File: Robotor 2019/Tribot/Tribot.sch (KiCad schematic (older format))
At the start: 63 parts, among them M1 Motor_DC, M2 Motor_DC, SW1 SW_Push, U1 AMS1117-3V3, U2 AMS1117-3V3, U3 AMS1117-5.0, Y1 Crystal, Y2 Crystal

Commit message: Nici nu mai stiu, am facut la scoala pe data de 23.07
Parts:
- removed C? (x2): 0.1uF, symbol Device:CP
- removed J?: Conn_01x04_Male, symbol Connector:Conn_01x04_Male
- added C3, C8: 100n, Capacitor_SMD:C_0805_2012Metric_Pad1.15x1.40mm_HandSolder, symbol Device:C
- added D9: LED, LED_SMD:LED_0805_2012Metric_Pad1.15x1.40mm_HandSolder, symbol Device:LED
- added J4, J5, J6: Conn_01x04_Female, symbol Connector:Conn_01x04_Female
- added J7, J8: Conn_01x03_Female, symbol Connector:Conn_01x03_Female
- added R20: 10K, Resistor_SMD:R_0805_2012Metric_Pad1.15x1.40mm_HandSolder, symbol Device:R
- added R5, R7: 1K, Resistor_SMD:R_0805_2012Metric_Pad1.15x1.40mm_HandSolder, symbol Device:R
- C1, C2, C4, C5, C6, C7, C9: footprint (none) -> Capacitor_SMD:C_0805_2012Metric_Pad1.15x1.40mm_HandSolder
- C12, C13, C15, C17, C18, C21, CP6: renamed from C?; footprint (none) -> Capacitor_SMD:C_0805_2012Metric_Pad1.15x1.40mm_HandSolder
- CP1: renamed from C?; footprint (none) -> Capacitor_SMD:CP_Elec_4x5.3
- CP2: renamed from C8; footprint (none) -> Capacitor_SMD:CP_Elec_6.3x7.7
- CP3, CP5: renamed from C?; footprint (none) -> Capacitor_SMD:CP_Elec_6.3x7.7
- CP4: renamed from C3; footprint (none) -> Capacitor_SMD:CP_Elec_6.3x7.7
- D1, D2, D3, D4, D5, D6, D7, D8: renamed from D?; footprint (none) -> Diode_SMD:D_0805_2012Metric_Pad1.15x1.40mm_HandSolder
- J1: renamed from J?; footprint (none) -> Connector_Wire:SolderWirePad_1x03_P5.715mm_Drill2mm
- R1, R10, R11, R2, R3, R4, R6, R8, R9: footprint (none) -> Resistor_SMD:R_0805_2012Metric_Pad1.15x1.40mm_HandSolder
- R12, R13, R14, R15, R16, R17, R18, R19: renamed from R?; footprint (none) -> Resistor_SMD:R_0805_2012Metric_Pad1.15x1.40mm_HandSolder
- SW1: footprint (none) -> Button_Switch_THT:SW_PUSH_6mm
- Y1, Y2: footprint (none) -> Crystal:Crystal_SMD_SeikoEpson_MA505-2Pin_12.7x5.1mm
- gave numbers to parts that had none: 7
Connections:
- net labels added: H1, H2, US1_IN, US1_OUT, US2_IN, US2_OUT, US3_IN, US3_OUT
- net labels removed: CLK, DIO
- wire segments 199 -> 228
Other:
- moved on the sheet: C12, CP1, J3, R10, R11, R3, R9, U2

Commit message: Assigned footprints to all parts. Arranged sensors in PCB schematic.
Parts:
- removed SW1: SW_Push, Button_Switch_THT:SW_PUSH_6mm, symbol Switch:SW_Push
- added J2: Conn_01x04_Female, Connector_PinSocket_2.54mm:PinSocket_1x04_P2.54mm_Vertical, symbol Connector:Conn_01x04_Female
- added JP1, JP2: Jumper, Connector_PinSocket_2.54mm:PinSocket_1x02_P2.54mm_Vertical, symbol Device:Jumper
- C15, C17, C18, C21: value C -> 10n
- CP2, CP3, CP4, CP5: footprint Capacitor_SMD:CP_Elec_6.3x7.7 -> Capacitor_SMD:CP_Elec_4x5.3
- CP6: footprint Capacitor_SMD:C_0805_2012Metric_Pad1.15x1.40mm_HandSolder -> Capacitor_SMD:CP_Elec_4x5.3
- D1, D2, D3, D4, D5, D6, D7, D8: footprint Diode_SMD:D_0805_2012Metric_Pad1.15x1.40mm_HandSolder -> Diode_THT:D_DO-15_P5.08mm_Vertical_AnodeUp
- J3: footprint (none) -> Connector_USB:USB_Mini-B_Lumberg_2486_01_Horizontal
- J4, J5, J6: footprint (none) -> Connector_PinHeader_2.54mm:PinHeader_1x04_P2.54mm_Vertical
- J7, J8: footprint (none) -> Connector_PinHeader_2.54mm:PinHeader_1x03_P2.54mm_Vertical
- M1, M2: footprint (none) -> Connector_Wire:SolderWirePad_1x02_P5.08mm_Drill1.5mm
- R12, R13, R14, R15, R16, R17, R18, R19: value R -> 220
- R20: value 10K -> R
- U6: footprint (none) -> Package_SO:HSOP-20-1EP_11.0x15.9mm_P1.27mm_SlugUp
- Y1: value Crystal -> 32.768Khz
- Y2: value Crystal -> 8Mhz
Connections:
- net labels added: BOOT1, CLK, DIO
- net labels removed: -5V
- wire segments 228 -> 231
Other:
- moved on the sheet: J8, R7

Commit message: The PCB for Tribot up to the point we realised we need a 2nd floor.
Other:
- moved on the sheet: C3, C8, CP5, CP6, D1, D2, D3, D4, D5, D6, D7, D8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

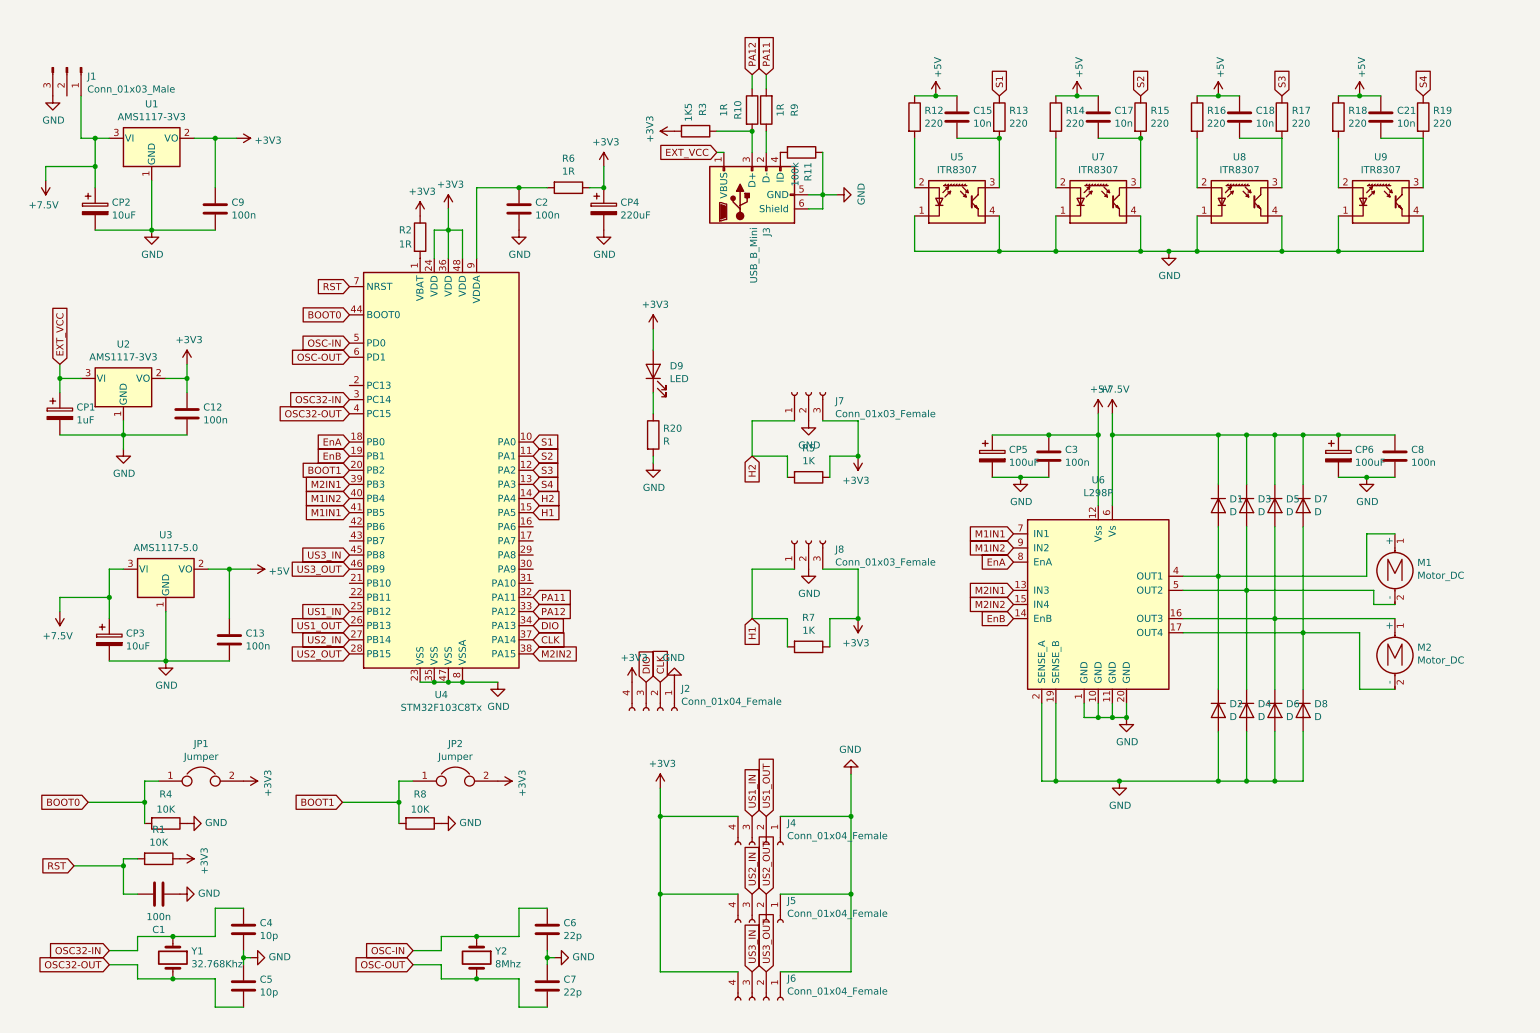
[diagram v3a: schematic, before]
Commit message: Updated electric schematic for tribot with 2 floors.
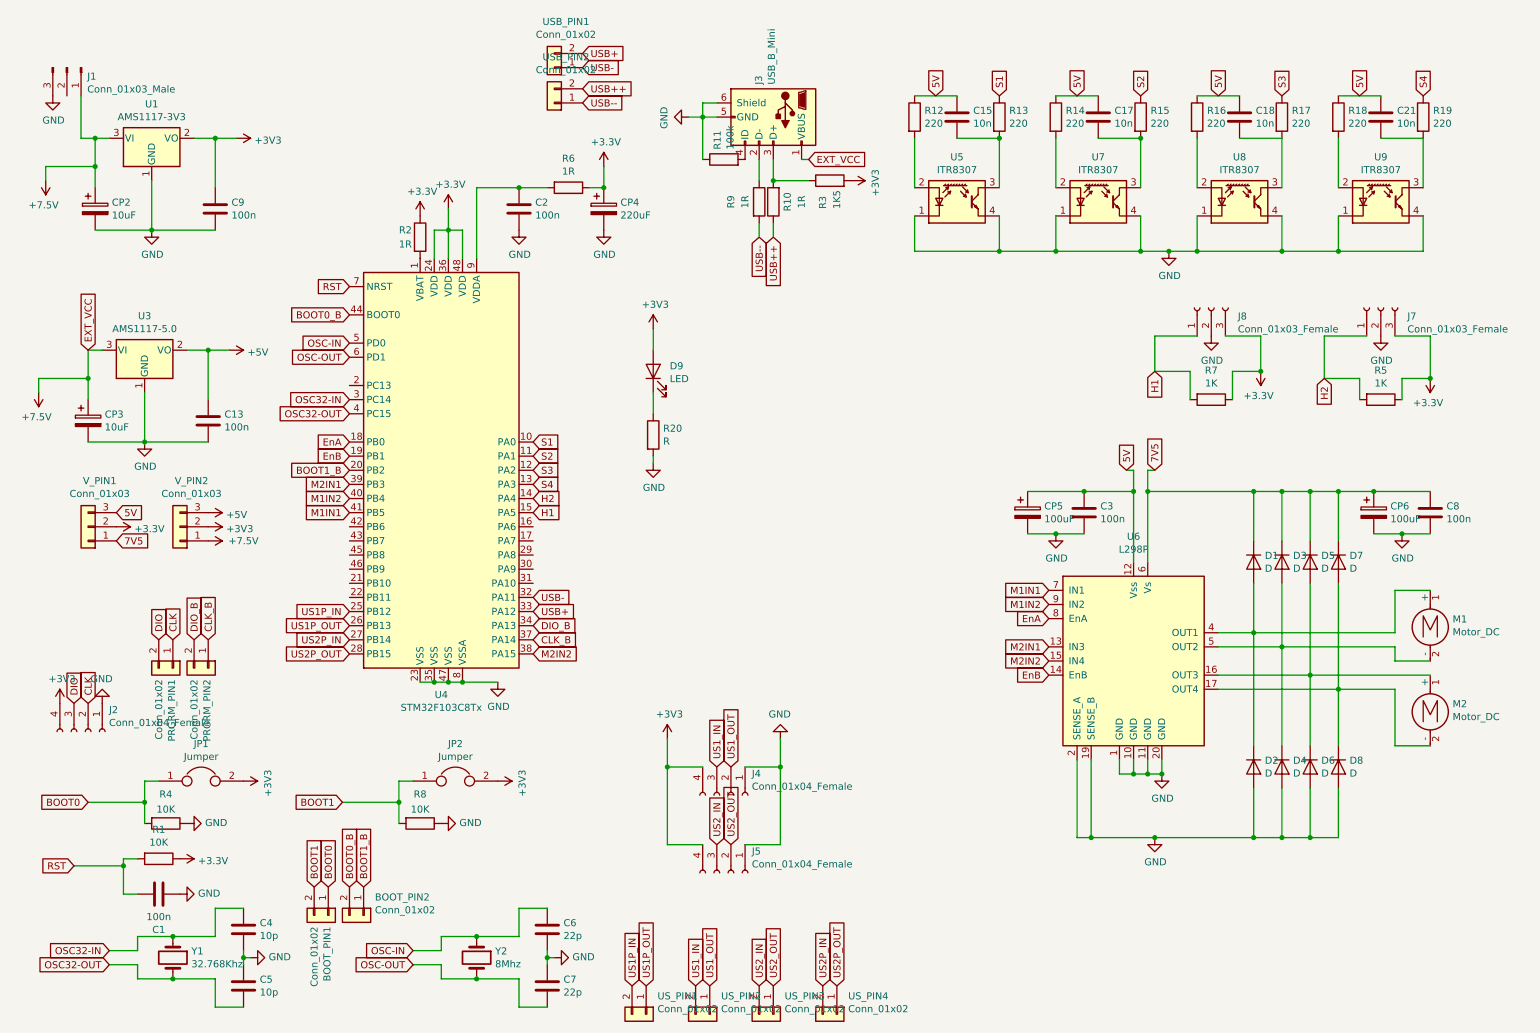
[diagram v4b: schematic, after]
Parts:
- removed C12: 100n, Capacitor_SMD:C_0805_2012Metric_Pad1.15x1.40mm_HandSolder, symbol Device:C
- removed CP1: 1uF, Capacitor_SMD:CP_Elec_4x5.3, symbol Device:CP
- removed J6: Conn_01x04_Female, Connector_PinHeader_2.54mm:PinHeader_1x04_P2.54mm_Vertical, symbol Connector:Conn_01x04_Female
- removed U2: AMS1117-3V3, Package_TO_SOT_SMD:SOT-223-3_TabPin2, symbol Regulator_Linear:AMS1117-5.0
- added BOOT_PIN1, BOOT_PIN2, PRGRM_PIN1, PRGRM_PIN2, USB_PIN1, USB_PIN2, US_PIN1, US_PIN2, US_PIN3, US_PIN4: Conn_01x02, Connector_PinHeader_2.54mm:PinHeader_1x02_P2.54mm_Vertical, symbol Connector_Generic:Conn_01x02
- added V_PIN1, V_PIN2: Conn_01x03, Connector_Wire:SolderWirePad_1x03_P5.715mm_Drill2mm, symbol Connector_Generic:Conn_01x03
- D1, D2, D3, D4, D5, D6, D7, D8: footprint Diode_THT:D_DO-15_P5.08mm_Vertical_AnodeUp -> Diode_THT:D_A-405_P5.08mm_Vertical_AnodeUp
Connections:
- net EXT_VCC is gone; now on net +7.5V: J3.1 (VBUS)
- net +3V3: now also V_PIN1.2 (Pin_2), V_PIN2.2 (Pin_2)
- net +5V: now also V_PIN2.3 (Pin_3); no longer C15.1, C17.1, C18.1, C21.1, C3.1, CP5.1, R12.1, R14.1, R16.1, R18.1, U6.12 (Vss)
- net +7.5V: now also V_PIN2.1 (Pin_1); no longer C8.1, CP6.1, D1.1 (K), D3.1 (K), D5.1 (K), D7.1 (K), U6.6 (Vs)
- net BOOT0: now also BOOT_PIN1.1 (Pin_1); no longer U4.44 (BOOT0)
- net BOOT1: now also BOOT_PIN1.2 (Pin_2); no longer U4.20 (PB2)
- net CLK: now also PRGRM_PIN1.1 (Pin_1); no longer U4.37 (PA14)
- net DIO: now also PRGRM_PIN1.2 (Pin_2); no longer U4.34 (PA13)
- net US1_IN: now also US_PIN2.2 (Pin_2); no longer U4.25 (PB12)
- net US1_OUT: now also US_PIN2.1 (Pin_1); no longer U4.26 (PB13)
- net US2_IN: now also US_PIN3.2 (Pin_2); no longer U4.27 (PB14)
- net US2_OUT: now also US_PIN3.1 (Pin_1); no longer U4.28 (PB15)
- net PA11 renamed USB-
- net USB-: now also USB_PIN1.1 (Pin_1); no longer R9.2
- net PA12 renamed USB+
- net USB+: now also USB_PIN1.2 (Pin_2); no longer R10.1
- net US3_IN: no longer names the net of U4.45 (PB8)
- net US3_OUT: no longer names the net of U4.46 (PB9)
- new net 5V: C15.1, C17.1, C18.1, C21.1, C3.1, CP5.1, R12.1, R14.1, R16.1, R18.1, U6.12 (Vss), V_PIN1.3 (Pin_3)
- new net 7V5: C8.1, CP6.1, D1.1 (K), D3.1 (K), D5.1 (K), D7.1 (K), U6.6 (Vs), V_PIN1.1 (Pin_1)
- new net BOOT0_B: BOOT_PIN2.2 (Pin_2), U4.44 (BOOT0)
- new net BOOT1_B: BOOT_PIN2.1 (Pin_1), U4.20 (PB2)
- new net CLK_B: PRGRM_PIN2.1 (Pin_1), U4.37 (PA14)
- new net DIO_B: PRGRM_PIN2.2 (Pin_2), U4.34 (PA13)
- new net US1P_IN: U4.25 (PB12), US_PIN1.2 (Pin_2)
- new net US1P_OUT: U4.26 (PB13), US_PIN1.1 (Pin_1)
- new net US2P_IN: U4.27 (PB14), US_PIN4.2 (Pin_2)
- new net US2P_OUT: U4.28 (PB15), US_PIN4.1 (Pin_1)
- new net USB++: R10.1, USB_PIN2.2 (Pin_2)
- new net USB--: R9.2, USB_PIN2.1 (Pin_1)
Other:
- moved on the sheet: C13, C3, C8, CP3, CP5, CP6, D1, D2, D3, D4, D5, D6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

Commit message: Bottom tribot circuit board.
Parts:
- removed V_PIN1, V_PIN2: Conn_01x03, Connector_Wire:SolderWirePad_1x03_P5.715mm_Drill2mm, symbol Connector_Generic:Conn_01x03
- added M_PIN1, M_PIN2, M_PIN3, M_PIN4: Conn_01x03, Connector_PinSocket_2.54mm:PinSocket_1x03_P2.54mm_Vertical, symbol Connector_Generic:Conn_01x03
- added V_PIN1, V_PIN2: Conn_01x02, Connector_Wire:SolderWirePad_1x02_P5.08mm_Drill1.5mm, symbol Connector_Generic:Conn_01x02
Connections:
- net 7V5 is gone; now on net +7.5V: C8.1, CP6.1, D1.1 (K), D3.1 (K), D5.1 (K), D7.1 (K), U6.6 (Vs)
- net +3V3: now also V_PIN2.1 (Pin_1); no longer CP4.1, J7.3 (Pin_3), J8.3 (Pin_3), R1.1, R2.1, R5.1, R6.1, R7.1, U4.24 (VDD), U4.36 (VDD), U4.48 (VDD)
- net +5V: now also C3.1, CP5.1, U6.12 (Vss), V_PIN2.2 (Pin_2)
- net 5V: now also V_PIN1.2 (Pin_2); no longer C3.1, CP5.1, U6.12 (Vss)
- net EnA: now also M_PIN2.1 (Pin_1); no longer U4.18 (PB0)
- net EnB: now also M_PIN4.1 (Pin_1); no longer U4.19 (PB1)
- net M1IN1: now also M_PIN2.2 (Pin_2); no longer U4.41 (PB5)
- net M1IN2: now also M_PIN2.3 (Pin_3); no longer U4.40 (PB4)
- net M2IN1: now also M_PIN4.2 (Pin_2); no longer U4.39 (PB3)
- net M2IN2: now also M_PIN4.3 (Pin_3); no longer U4.38 (PA15)
- new net 3V3: CP4.1, J7.3 (Pin_3), J8.3 (Pin_3), R1.1, R2.1, R5.1, R6.1, R7.1, U4.24 (VDD), U4.36 (VDD), U4.48 (VDD), V_PIN1.1 (Pin_1)
- new net EnA_B: M_PIN1.1 (Pin_1), U4.18 (PB0)
- new net EnB_B: M_PIN3.1 (Pin_1), U4.19 (PB1)
- new net M1IN1_B: M_PIN1.2 (Pin_2), U4.41 (PB5)
- new net M1IN2_B: M_PIN1.3 (Pin_3), U4.40 (PB4)
- new net M2IN1_B: M_PIN3.2 (Pin_2), U4.39 (PB3)
- new net M2IN2_B: M_PIN3.3 (Pin_3), U4.38 (PA15)
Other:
- moved on the sheet: J2

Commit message: Tribot bottom circuit board final version (hopefully)
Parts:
- added D10: DIODE, Diode_THT:D_A-405_P5.08mm_Vertical_AnodeUp, symbol Simulation_SPICE:DIODE
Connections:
- net +7.5V: now also D10.2 (K); no longer J3.1 (VBUS)
- new net EXT_VCC: D10.1 (A), J3.1 (VBUS)
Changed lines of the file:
@@
 Text GLabel 6200 1450 2    50   Input ~ 0
 EXT_VCC
-Text GLabel 1100 2800 1    50   Input ~ 0
+Text GLabel 650  1300 3    50   Input ~ 0
 EXT_VCC
 $Comp
@@
 Text GLabel 5750 4000 1    50   Input ~ 0
 M1IN2_B
+$Comp
+L Simulation_SPICE:DIODE D10
+U 1 1 5D3C17DD
+P 900 1300
+F 0 "D10" H 900 1517 50  0000 C CNN
+F 1 "DIODE" H 900 1426 50  0000 C CNN
+F 2 "Diode_THT:D_A-405_P5.08mm_Vertical_AnodeUp" H 900 1300 50  0001 C CNN
+F 3 "~" H 900 1300 50  0001 C CNN
+F 4 "Y" H 900 1300 50  0001 L CNN "Spice_Netlist_Enabled"
+F 5 "V" H 900 1300 50  0001 L CNN "Spice_Primitive"
+	1    900  1300
+	1    0    0    -1
+$EndComp
+Connection ~ 1050 1300
+Wire Wire Line
+	650  1300 750  1300
 $EndSCHEMATC

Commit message: Small tweaks to vias, paths, added parts lists.
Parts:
- added SW1, SW2: SW_Push, Button_Switch_SMD:SW_Push_1P1T_NO_6x6mm_H9.5mm, symbol Switch:SW_Push
- added SW_PIN1, SW_PIN2: Conn_01x02, Connector_PinSocket_2.54mm:PinSocket_1x02_P2.54mm_Vertical, symbol Connector_Generic:Conn_01x02
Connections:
- net GND: now also SW1.1, SW2.1
- net at U4.16 (PA6): now also SW_PIN1.1 (Pin_1)
- net at U4.17 (PA7): now also SW_PIN1.2 (Pin_2)
- new net: SW2.2, SW_PIN2.1 (Pin_1)
- new net: SW1.2, SW_PIN2.2 (Pin_2)
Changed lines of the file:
@@
 Wire Wire Line
 	650  1300 750  1300
+$Comp
+L Switch:SW_Push SW2
+U 1 1 5D4D043A
+P 7000 2800
+F 0 "SW2" V 6954 2948 50  0000 L CNN
+F 1 "SW_Push" V 7045 2948 50  0000 L CNN
+F 2 "Button_Switch_SMD:SW_Push_1P1T_NO_6x6mm_H9.5mm" H 7000 3000 50  0001 C CNN
+F 3 "~" H 7000 3000 50  0001 C CNN
+	1    7000 2800
+	0    1    1    0
+$EndComp
+$Comp
+L Switch:SW_Push SW1
+U 1 1 5D4D1350
+P 6400 2800
+F 0 "SW1" V 6354 2948 50  0000 L CNN
+F 1 "SW_Push" V 6445 2948 50  0000 L CNN
+F 2 "Button_Switch_SMD:SW_Push_1P1T_NO_6x6mm_H9.5mm" H 6400 3000 50  0001 C CNN
+F 3 "~" H 6400 3000 50  0001 C CNN
+	1    6400 2800
+	0    1    1    0
+$EndComp
+Wire Wire Line
+	6400 2600 6700 2600
+$Comp
+L power:GND #PWR0113
+U 1 1 5D4E8556
+P 6700 2600
+F 0 "#PWR0113" H 6700 2350 50  0001 C CNN
+F 1 "GND" H 6705 2427 50  0000 C CNN
+F 2 "" H 6700 2600 50  0001 C CNN
+F 3 "" H 6700 2600 50  0001 C CNN
+	1    6700 2600
+	-1   0    0    1
+$EndComp
+Connection ~ 6700 2600
+Wire Wire Line
+	6700 2600 7000 2600
+$Comp
+L Connector_Generic:Conn_01x02 SW_PIN2
+U 1 1 5D4E9E36
+P 6750 3200
+F 0 "SW_PIN2" H 6830 3192 50  0000 L CNN
+F 1 "Conn_01x02" H 6830 3101 50  0000 L CNN
+F 2 "Connector_PinSocket_2.54mm:PinSocket_1x02_P2.54mm_Vertical" H 6750 3200 50  0001 C CNN
+F 3 "~" H 6750 3200 50  0001 C CNN
+	1    6750 3200
+	0    1    1    0
+$EndComp
+Wire Wire Line
+	6400 3000 6650 3000
+Wire Wire Line
+	7000 3000 6750 3000
+$Comp
+L Connector_Generic:Conn_01x02 SW_PIN1
+U 1 1 5D505287
+P 4450 4050
+F 0 "SW_PIN1" H 4530 4042 50  0000 L CNN
+F 1 "Conn_01x02" H 4530 3951 50  0000 L CNN
+F 2 "Connector_PinSocket_2.54mm:PinSocket_1x02_P2.54mm_Vertical" H 4450 4050 50  0001 C CNN
+F 3 "~" H 4450 4050 50  0001 C CNN
+	1    4450 4050
+	1    0    0    -1
+$EndComp
 $EndSCHEMATC
